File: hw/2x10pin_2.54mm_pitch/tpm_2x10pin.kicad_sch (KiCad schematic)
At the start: 9 parts, among them J1 Conn_02x10_Odd_Even, U1 SLB9665

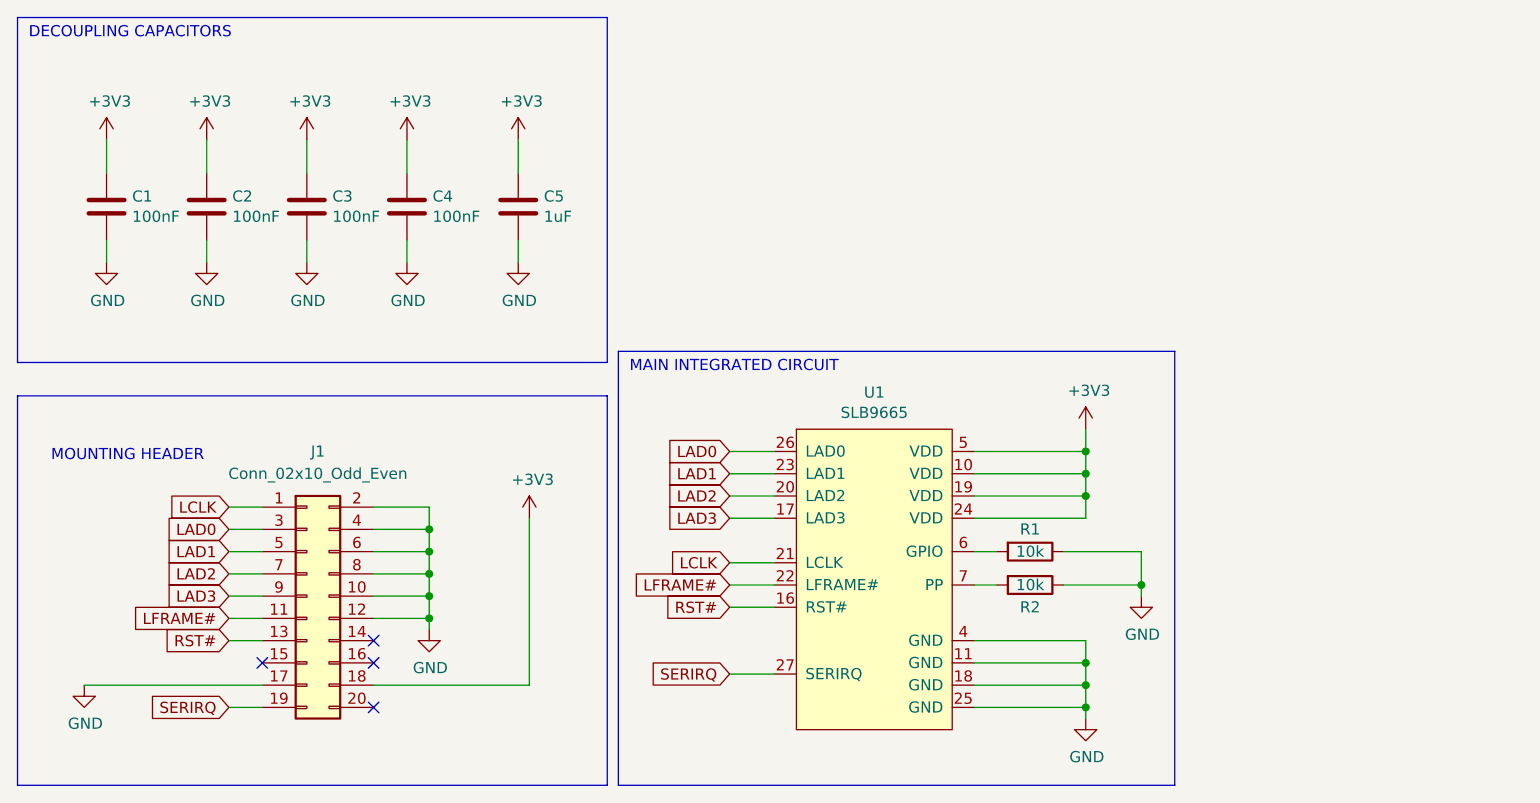
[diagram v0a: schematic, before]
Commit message: hw/2x10pin_2.54mm_pitch: Update proejct files with proper BOM
Signed-off-by: Michał Żygowski <michal.zygowski@3mdeb.com>
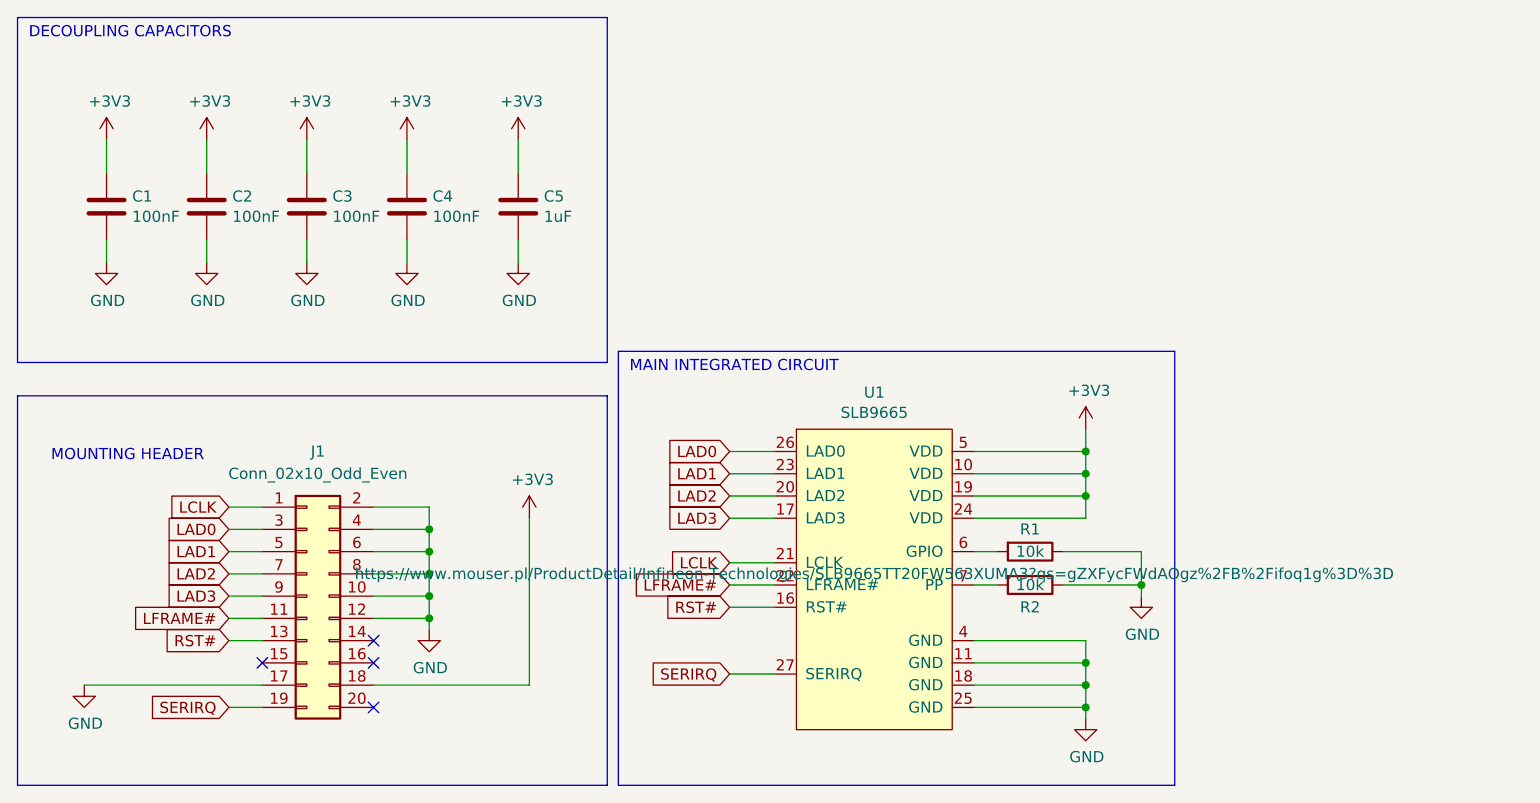
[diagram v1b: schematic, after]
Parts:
- U1: Supplier and ref (none) -> https://www.mouser.pl/ProductDetail/Infineon-Technologies/S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
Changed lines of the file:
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@@
       (effects (font (size 1.27 1.27)) hide)
+    )
+    (property "Supplier and ref" "https://www.mouser.pl/ProductDetail/Infineon-Technologies/SLB9665TT20FW563XUMA3?qs=gZXFycFWdAOgz%2FB%2Fifoq1g%3D%3D" (at 248.92 139.7 0)
+      (effects (font (size 1.27 1.27)))
     )
     (pin "26")

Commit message: Add UserComments layer with board setup and characteristics
Signed-off-by: Michał Żygowski <michal.zygowski@3mdeb.com>
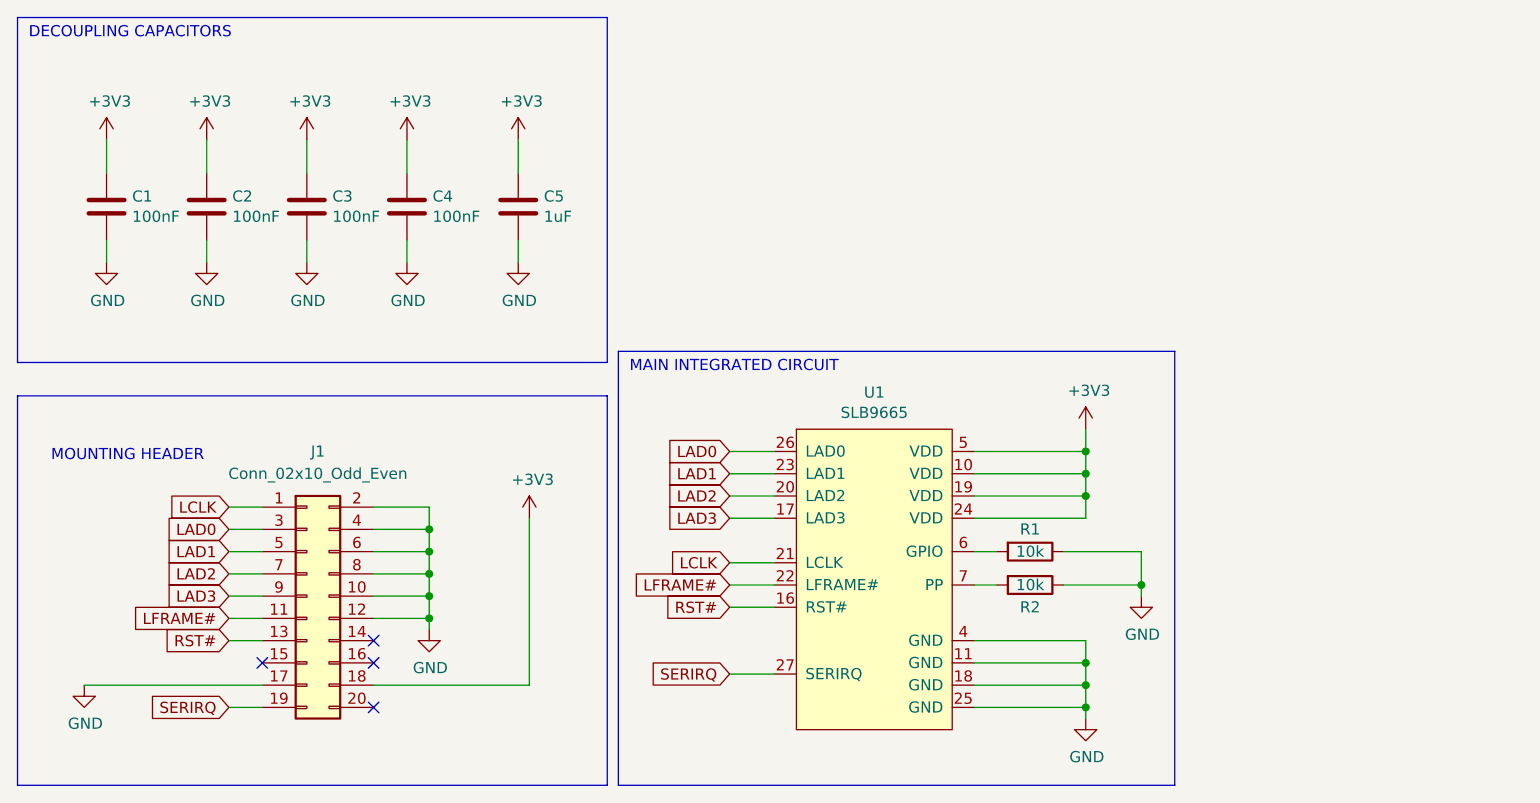
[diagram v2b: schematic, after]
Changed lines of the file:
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@@
       (effects (font (size 1.27 1.27)) hide)
     )
-    (property "Supplier and ref" "https://www.mouser.pl/ProductDetail/Infineon-Technologies/SLB9665TT20FW563XUMA3?qs=gZXFycFWdAOgz%2FB%2Fifoq1g%3D%3D" (at 248.92 139.7 0)
-      (effects (font (size 1.27 1.27)))
+    (property "Supplier and ref" "https://www.mouser.pl/ProductDetail/Infineon-Technologies/SLB9665TT20FW563XUMA3?qs=gZXFycFWdAOgz%2FB%2Fifoq1g%3D%3D" (at 234.95 160.02 0)
+      (effects (font (size 1.27 1.27)) hide)
     )
     (pin "26")
